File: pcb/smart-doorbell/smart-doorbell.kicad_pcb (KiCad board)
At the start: 2 copper layers, 59 x 91 mm, 57 parts, among them J1 Conn_01x02_Pin, J2 USB_C_Receptacle_USB2.0_16P, J3 Conn_01x24, J4 Conn_01x06, J6 Conn_01x02_Pin, J7 Conn_01x03, J8 Conn_01x04, U1 ESP32-S3-WROOM-2, U2 MCP73831-2-OT, U3 AP2112K-3.3, U4 MAX98357A, U5 SRV05-4, U6 XC6206P152MR, U7 XC6206P282MR

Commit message: Update Rev B camera hardware outputs
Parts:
- added R15: 680, Resistor_SMD:R_0603_1608Metric, F.Cu at (149.8, 86.0)
- added R16: 3.9k, Resistor_SMD:R_0603_1608Metric, F.Cu at (151.6, 86.0)
- added R17: 10k, Resistor_SMD:R_0603_1608Metric, F.Cu at (150.6, 88.4)
- added R18: 56k, Resistor_SMD:R_0603_1608Metric, F.Cu at (128.8, 88.0)
- added R19: 10k, Resistor_SMD:R_0603_1608Metric, F.Cu at (128.0, 85.8)
- added R20: 56k, Resistor_SMD:R_0603_1608Metric, F.Cu at (129.9, 85.8)
- REF** (x4): value MountingHole_2.2mm_M2 -> MountingHole_2.7mm_M2.5; footprint MountingHole:MountingHole_2.2mm_M2 -> MountingHole:MountingHole_2.7mm_M2.5
- U1: value ESP32-S3-WROOM-2 -> ESP32-S3-WROOM-1; footprint RF_Module:ESP32-S3-WROOM-2 -> RF_Module:ESP32-S3-WROOM-1
- moved R14 4.37 mm to (138.0, 91.2)
- moved C22 4.37 mm to (138.0, 89.5)
- moved C23 4.10 mm to (144.6, 89.5)
- moved C21 4.10 mm to (134.9, 89.5)
- moved C25 4.10 mm to (134.9, 91.2)
- moved C9 4.10 mm to (141.9, 90.3)
- moved C20 4.10 mm to (144.6, 91.0)
- moved C3 3.91 mm to (136.9, 108.3)
- moved U3 3.91 mm to (140.0, 108.3)
- moved C1 3.89 mm to (124.7, 58.9)
- moved C2 3.89 mm to (124.7, 56.5)
- moved C15 3.10 mm to (134.9, 100.7)
- moved C17 3.10 mm to (142.1, 100.4)
- moved U6 3.10 mm to (136.8, 98.3)
- moved U7 3.10 mm to (144.0, 98.3)
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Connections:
- C22 pad 2: +3V3 -> +2V8
- J3 pad 11: +3V3 -> +2V8
- J3 pad 13: /CAM_XCLK -> /CAM_XCLK_2V8
- J3 pad 6: /CAM_RST -> /CAM_RST_2V8
- J3 pad 8: /CAM_PWDN -> /CAM_PWDN_2V8
- R13 pad 2: +3V3 -> +2V8
- R14 pad 2: +3V3 -> +2V8
- U1 pad 15: /PIR_OUT -> unconnected-(U1-IO3-Pad15)
- U1 pad 35: unconnected-(U1-MTMS/IO42-Pad35) -> /PIR_OUT
- U1 pad 36: unconnected-(U1-RXD0/IO44-Pad36) -> /AMP_EN
- U1 pad 37: /AMP_EN -> unconnected-(U1-TXD0-Pad37)
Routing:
- net +2V8: track 33.7 -> 80.2 mm, vias 4 -> 6
- net /GPIO4: track 108.2 -> 136.5 mm, vias 4 -> 5
- net /CAM_RST_2V8: track 0.00 -> 27.0 mm, vias 0 -> 3
- net /CAM_XCLK_2V8: track 0.00 -> 24.2 mm, vias 0 -> 2
- net /GPIO5: track 106.8 -> 126.7 mm, vias 8 -> 9
- net /CAM_PWDN: track 9.62 -> 29.5 mm, vias 0 -> 2
- net GND: track 141.9 -> 161.4 mm, vias 18 -> 22
- net /CAM_PWDN_2V8: track 0.00 -> 16.9 mm, vias 0 -> 2
- net +1V5: track 52.1 -> 37.5 mm, vias 2 -> 5
- net /CAM_XCLK: track 9.40 -> 19.5 mm, vias 0 -> 2
- net /CAM_RST: track 23.4 -> 32.1 mm
- net /CAM_SCL: track 30.0 -> 37.2 mm, vias 4 -> 6
- net /PIR_OUT: track 34.4 -> 28.2 mm
- net +BATT: track 192.2 -> 198.3 mm
- net +3V3: track 248.6 -> 254.6 mm
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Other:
- board text added: "Smart Doorbell Project Rev B Caleb Habesh"
- board text removed: "Smart Doorbell Project v1 Caleb Habesh"

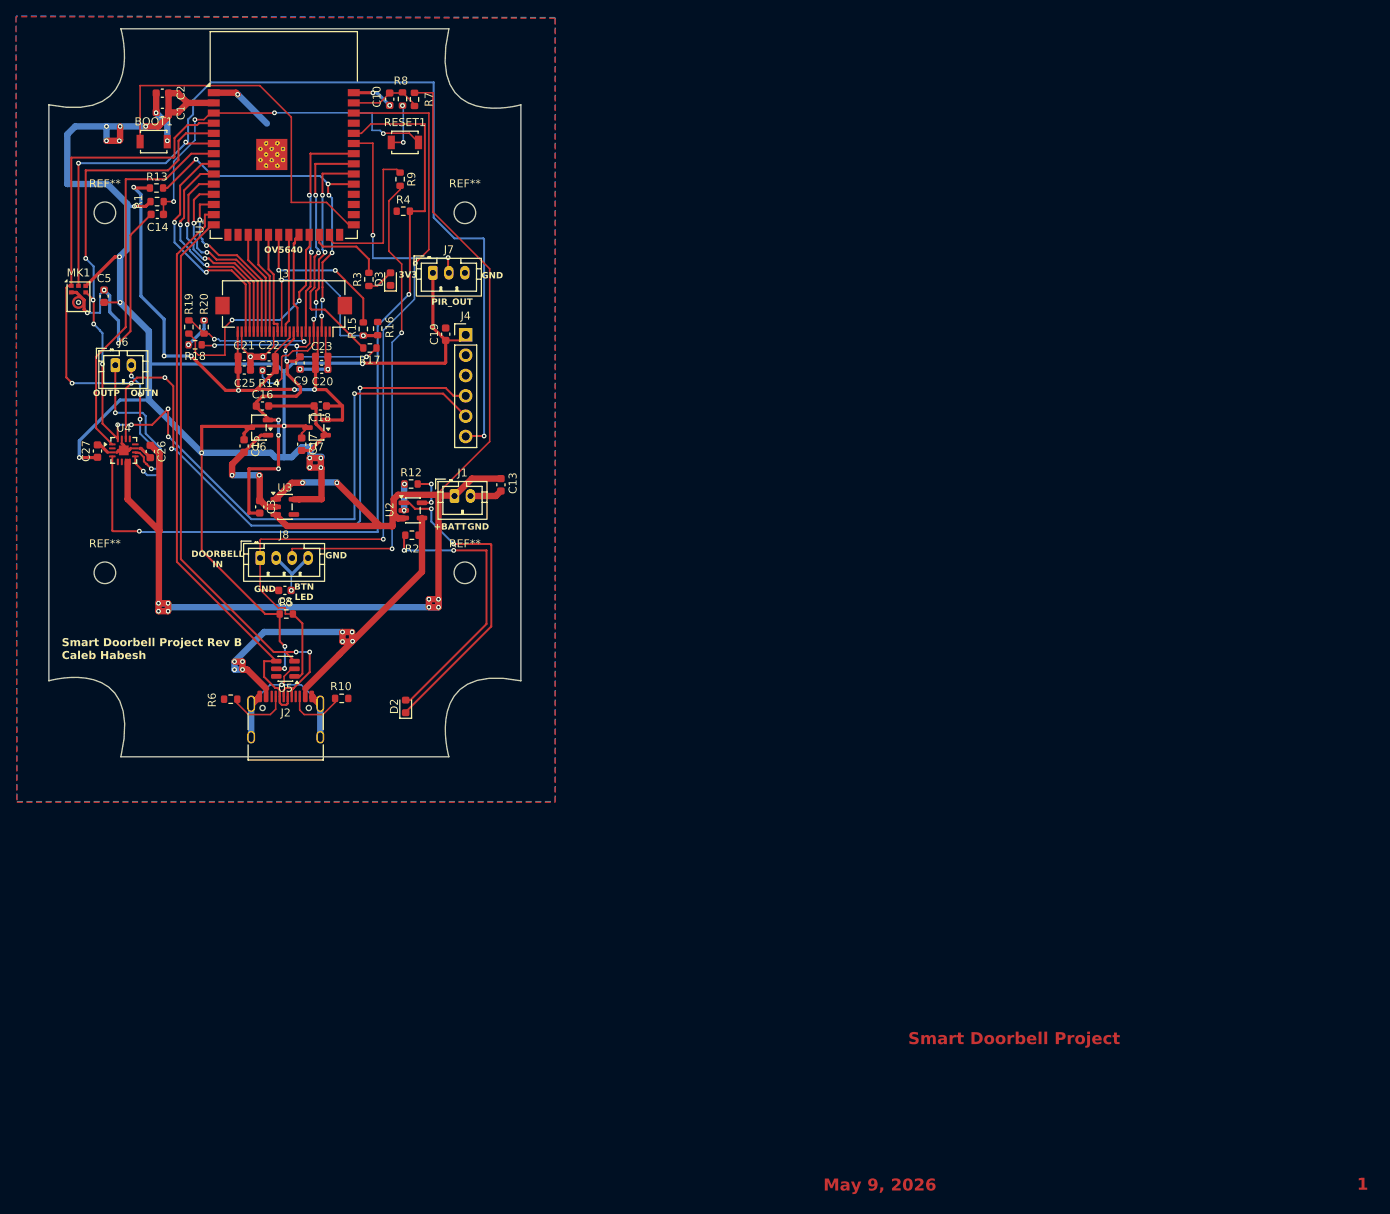
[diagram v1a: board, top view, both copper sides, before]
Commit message: Release Smart Doorbell Rev B PCB order snapshot
Record the exact JLCPCB Gerber, BOM, and CPL files submitted on 2026-07-15, including project-local part/placement corrections and the verified native top-mask repair. Preserve the routed KiCad sources, production netlists, custom power footprints, camera documentation, assembly exclusions, and release hashes used for the five-board first-article order.
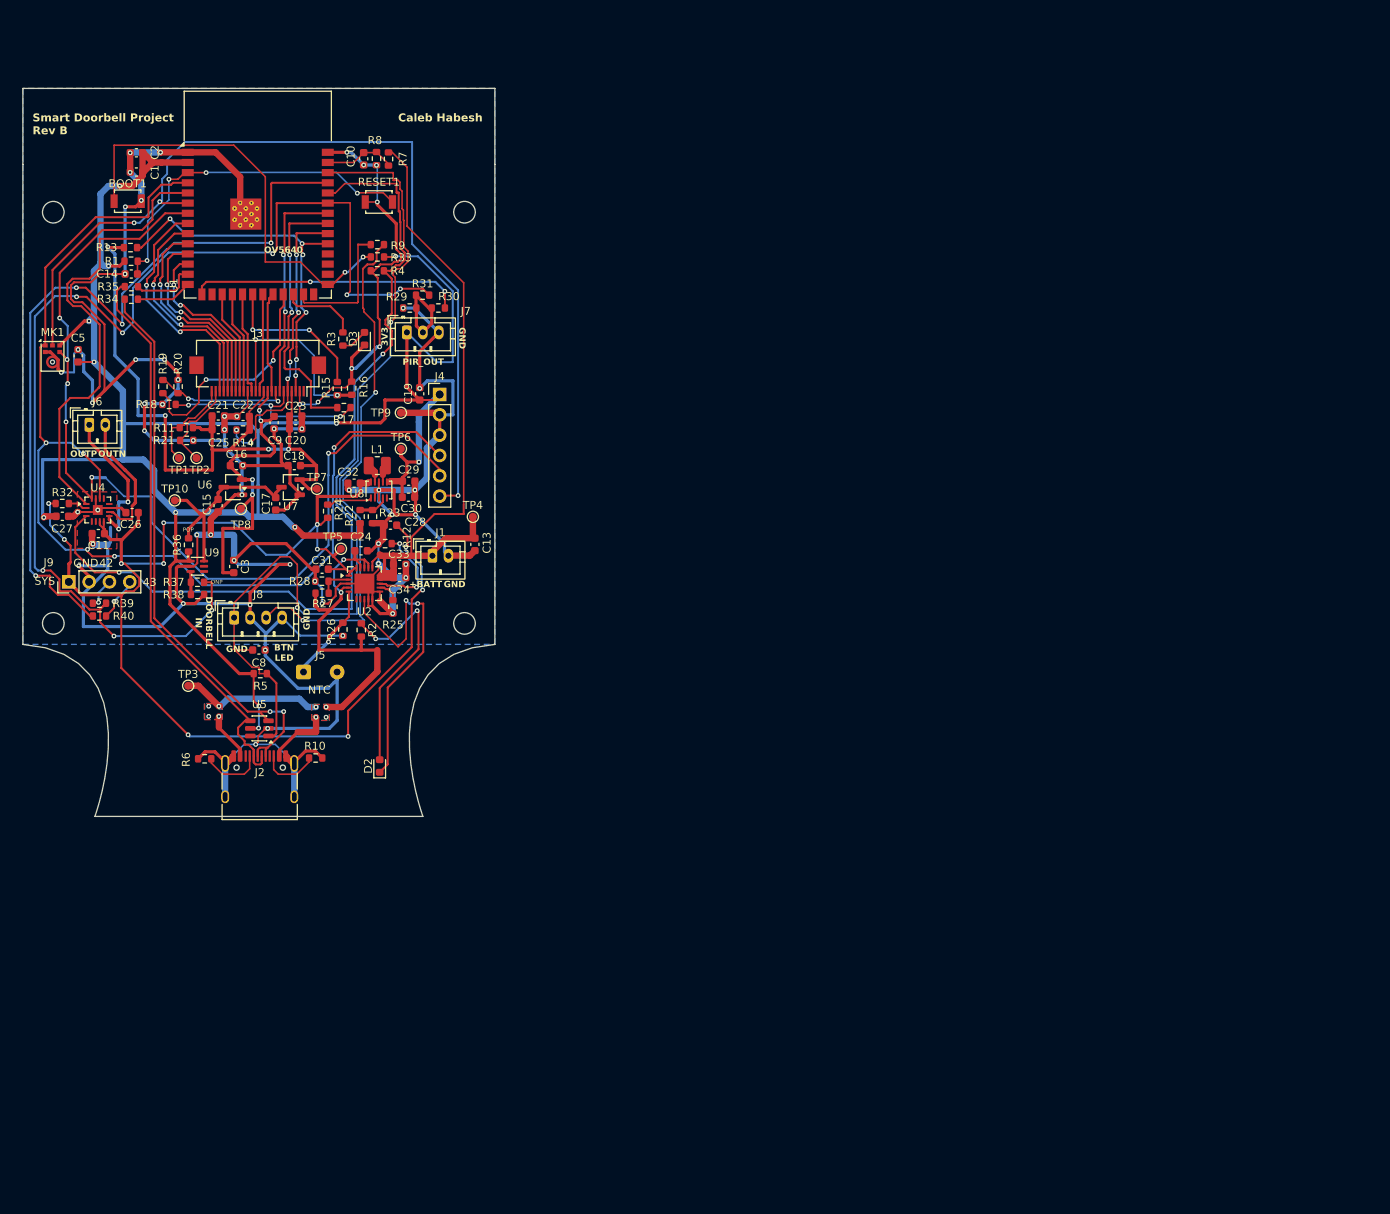
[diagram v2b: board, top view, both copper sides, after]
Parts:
- removed REF** (x4): MountingHole_2.7mm_M2.5, MountingHole:MountingHole_2.7mm_M2.5
- removed U3: AP2112K-3.3, Package_TO_SOT_SMD:SOT-23-5
- added C11: 0.1u, Capacitor_SMD:C_0603_1608Metric, F.Cu at (116.7, 111.6)
- added C24: 22u, Capacitor_SMD:C_0603_1608Metric, F.Cu at (149.5, 113.8)
- added C28: 0.1u, Capacitor_SMD:C_0603_1608Metric, F.Cu at (153.2, 110.5)
- added C29: 22u, Capacitor_SMD:C_0603_1608Metric, F.Cu at (155.5, 105.0)
- added C30: 0.1u, Capacitor_SMD:C_0603_1608Metric, F.Cu at (155.4, 107.0)
- added C31: 22u, Capacitor_SMD:C_0603_1608Metric, F.Cu at (144.7, 116.0)
- added C32: 10u, Capacitor_SMD:C_0603_1608Metric, F.Cu at (148.7, 105.3)
- added C33: 10u, Capacitor_SMD:C_0603_1608Metric, F.Cu at (154.3, 117.1)
- added C34: 10u, Capacitor_SMD:C_0603_1608Metric, F.Cu at (154.3, 115.5)
- added H1: MountingHole_2.7mm_M2.5, MountingHole:MountingHole_2.7mm_M2.5, F.Cu at (111.0, 71.4)
- added H2: MountingHole_2.7mm_M2.5, MountingHole:MountingHole_2.7mm_M2.5, F.Cu at (162.4, 71.4)
- added H3: MountingHole_2.7mm_M2.5, MountingHole:MountingHole_2.7mm_M2.5, F.Cu at (111.0, 122.8)
- added H4: MountingHole_2.7mm_M2.5, MountingHole:MountingHole_2.7mm_M2.5, F.Cu at (162.4, 122.8)
- added J5: NTC_OPTION, Connector_Wire:SolderWire-0.25sqmm_1x02_P4.2mm_D0.65mm_OD1.7mm, F.Cu at (142.3, 128.9)
- added J9: Conn_01x04, Connector_PinHeader_2.54mm:PinHeader_1x04_P2.54mm_Vertical, F.Cu at (113.0, 117.6)
- added L1: 0.47u, Inductor_SMD:L_1008_2520Metric, F.Cu at (151.6, 103.1)
- added R11: 0, Resistor_SMD:R_0603_1608Metric, F.Cu at (127.7, 98.3)
- added R21: 0, Resistor_SMD:R_0603_1608Metric, F.Cu at (127.7, 100.0)
- added R22: 511k, Resistor_SMD:R_0603_1608Metric, F.Cu at (149.4, 109.5)
- added R23: 91k, Resistor_SMD:R_0603_1608Metric, F.Cu at (150.9, 109.5)
- added R24: 100k, Resistor_SMD:R_0603_1608Metric, F.Cu at (145.3, 108.8)
- added R25: 25k, Resistor_SMD:R_0603_1608Metric, F.Cu at (153.5, 120.8)
- added R26: 10k, Resistor_SMD:R_0603_1608Metric, F.Cu at (147.2, 123.6)
- added R27: 330k, Resistor_SMD:R_0603_1608Metric, F.Cu at (144.7, 119.0)
- added R28: 110k, Resistor_SMD:R_0603_1608Metric, F.Cu at (144.6, 117.5)
- added R29: 100k, Resistor_SMD:R_0603_1608Metric, F.Cu at (155.6, 83.4)
- added R30: 1k, Resistor_SMD:R_0603_1608Metric, F.Cu at (159.2, 83.4)
- added R31: 1k, Resistor_SMD:R_0603_1608Metric, F.Cu at (157.2, 81.8)
- added R32: 0, Resistor_SMD:R_0603_1608Metric, F.Cu at (112.2, 107.8)
- added R33: 10k, Resistor_SMD:R_0603_1608Metric, F.Cu at (151.6, 77.0)
- added R34: 22, Resistor_SMD:R_0603_1608Metric, F.Cu at (120.8, 82.3)
- added R35: 22, Resistor_SMD:R_0603_1608Metric, F.Cu at (120.8, 80.7)
- added R36: 0, Resistor_SMD:R_0603_1608Metric, F.Cu at (128.0, 113.0)
- added R37: 1k, Resistor_SMD:R_0603_1608Metric, F.Cu at (129.1, 117.7)
- added R38: 100k, Resistor_SMD:R_0603_1608Metric, F.Cu at (129.1, 119.2)
- added R39: 1k, Resistor_SMD:R_0603_1608Metric, F.Cu at (116.8, 120.3)
- added R40: 1k, Resistor_SMD:R_0603_1608Metric, F.Cu at (116.8, 121.9)
- added TP1: TestPoint, TestPoint:TestPoint_Pad_D1.0mm, F.Cu at (126.8, 102.2)
- added TP10: TestPoint, TestPoint:TestPoint_Pad_D1.0mm, F.Cu at (126.2, 107.5)
- added TP2: TestPoint, TestPoint:TestPoint_Pad_D1.0mm, F.Cu at (128.9, 102.2)
- added TP3: TestPoint, TestPoint:TestPoint_Pad_D1.0mm, F.Cu at (127.9, 130.6)
- added TP4: TestPoint, TestPoint:TestPoint_Pad_D1.0mm, F.Cu at (163.5, 109.5)
- added TP5: TestPoint, TestPoint:TestPoint_Pad_D1.0mm, F.Cu at (147.0, 113.5)
- added TP6: TestPoint, TestPoint:TestPoint_Pad_D1.0mm, F.Cu at (154.5, 101.0)
- added TP7: TestPoint, TestPoint:TestPoint_Pad_D1.0mm, F.Cu at (144.0, 106.0)
- added TP8: TestPoint, TestPoint:TestPoint_Pad_D1.0mm, F.Cu at (134.5, 108.5)
- added TP9: TestPoint, TestPoint:TestPoint_Pad_D1.0mm, F.Cu at (154.5, 96.5)
- added U8: TPS63802DLAR, smart-doorbell-power:TPS63802DLAR_DLA0010A, F.Cu at (151.8, 106.2)
- added U9: TPS22919DCK, Package_TO_SOT_SMD:SOT-363_SC-70-6, F.Cu at (129.1, 115.7)
- C27: value 10u -> 22u
- R12: value 2k -> 4.7k
- U2: value MCP73831-2-OT -> MCP73871T-2AAI/ML; footprint Package_TO_SOT_SMD:SOT-23-5 -> Package_DFN_QFN:QFN-20-1EP_4x4mm_P0.5mm_EP2.5x2.5mm
- U4: footprint Package_DFN_QFN:TQFN-16-1EP_3x3mm_P0.5mm_EP1.23x1.23mm -> smart-doorbell-power:MAX98357A_TQFN-16-1EP_3x3mm_P0.5mm_EP1.23x1.23mm
- U6: value XC6206P152MR -> DS8561-15S3
- moved R2 13.4 mm to (149.6, 123.7), turned to -90 degrees
- moved U2 11.0 mm to (149.9, 117.8)
- moved C27 9.26 mm to (112.2, 109.4), turned to 0 degrees
- moved R9 8.66 mm to (151.6, 75.5), turned to 0 degrees
- moved D2 8.13 mm to (151.8, 140.7)
- moved R10 8.13 mm to (143.8, 139.7)
- moved C1 8.13 mm to (121.4, 66.4)
- moved C10 8.13 mm to (149.8, 64.8)
- moved C13 8.13 mm to (163.8, 113.0)
- moved C14 8.13 mm to (120.8, 79.2)
- moved C17 8.13 mm to (138.8, 107.9)
- moved C19 8.13 mm to (156.8, 94.1)
- moved C20 8.13 mm to (141.3, 98.5)
- moved C21 8.13 mm to (131.7, 96.9)
- moved C22 8.13 mm to (134.8, 97.0)
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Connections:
- C15 pad 1: +3V3 -> /CAM_3V3
- C17 pad 1: +3V3 -> /CAM_3V3
- C26 pad 1: +BATT -> /SYS
- J2 pad A6: /GPIO20 -> /U5_IO2
- J2 pad A7: /GPIO19 -> /U5_IO3
- J2 pad B6: /GPIO20 -> /U5_IO2
- J2 pad B7: /GPIO19 -> /U5_IO3
- J3 pad 23: GND -> Net-(J3-Pin_23)
- J3 pad 24: +2V8 -> Net-(J3-Pin_24)
- J7 pad 2: /PIR_OUT -> /PIR_SENSOR_OUT
- R12 pad 2: Net-(U2-PROG) -> Net-(U2-PROG1)
- U1 pad 15: unconnected-(U1-IO3-Pad15) -> /PIR_WAKE
- U1 pad 35: /PIR_OUT -> /GPIO42_AUX
- U1 pad 37: unconnected-(U1-TXD0-Pad37) -> /GPIO43_AUX
- U2 pad 1: Net-(D2-K) -> /SYS
- U2 pad 2: GND -> Net-(U2-VPCC)
- U2 pad 3: +BATT -> GND
- U2 pad 5: Net-(U2-PROG) -> /BATT_THERM
- U4 pad 2: unconnected-(U4-GAIN_SLOT-Pad2) -> Net-(U4-GAIN_SLOT)
- U4 pad 7: +BATT -> /SYS
- U4 pad 8: +BATT -> /SYS
- U5 pad 3: /GPIO20 -> /U5_IO2
- U5 pad 4: /GPIO19 -> /U5_IO3
- U6 pad 3: +3V3 -> /CAM_3V3
- U7 pad 3: +3V3 -> /CAM_3V3
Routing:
- net GND: track 161.4 -> 529.4 mm, vias 22 -> 59
- net /SYS: track 0.00 -> 171.1 mm, vias 0 -> 11
- net /GPIO42_AUX: track 0.00 -> 144.5 mm, vias 0 -> 8
- net +BATT: track 198.3 -> 86.3 mm, vias 10 -> 0
- net /GPIO43_AUX: track 0.00 -> 97.4 mm, vias 0 -> 4
- net /U5_IO2: track 0.00 -> 72.7 mm, vias 0 -> 2
- net /U5_IO3: track 0.00 -> 71.3 mm
- net /GPIO20: track 74.8 -> 7.21 mm, vias 2 -> 0
- net /GPIO19: track 73.3 -> 8.17 mm
- net /PIR_WAKE: track 0.00 -> 34.3 mm, vias 0 -> 2
- net /PIR_OUT: track 28.2 -> 0.00 mm, vias 2 -> 0
- net /CAM_3V3: track 0.00 -> 27.1 mm
- net +5V: track 55.2 -> 77.7 mm, vias 8 -> 10
- net /BATT_THERM: track 0.00 -> 12.4 mm, vias 0 -> 1
- net /DOORBELL_IN: track 103.9 -> 116.3 mm
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- added copper zone on B.Cu, net +5V
- added copper zone on F.Cu, net +5V
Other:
- outline, holes or cut-outs redrawn
- board text added: "42"
- board text added: "43"
- board text added: "Caleb Habesh"
- board text added: "DNP"
- board text added: "NTC"
- board text added: "POP"
- board text added: "SYS"
- board text added: "Smart Doorbell Project Rev B"
- board text removed: "1"
- board text removed: "May 9, 2026"
- board text removed: "Smart Doorbell Project"
- board text removed: "Smart Doorbell Project Rev B Caleb Habesh"
